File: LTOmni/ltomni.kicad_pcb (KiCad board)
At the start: 2 copper layers, 114.3 x 76.2 mm, 136 parts, among them J1 USB_C_Receptacle, J2 USB_C_Receptacle, J3 TC2030-IDC, J4 D4, J5 D5, J6 A6, J7 A7, J8 B0, K0 K00, K1 K01, K10 K10, K10b1 K10b, K11 K11, K12 K12, K13 K13, K14 K14, K15 K15, K15b1 K15b, K2 K02, K20 K20, K21 K21, K22 K22, K23 K23, K24 K24, K25 K25, K3 K03, K30 K30, K30b1 K30b, K30b2 K30b2, K31 K31, K31b2 K31b, K31c1 K31c, K32 K32, K32b1 K32b1, K32b2 K32b2, K33 K33, K33b1 K33b, K34 K34, K34b1 K34b, K34c1 K34c, K35 K35, K35b1 K35b, K35c2 K35c, K4 K04, K5 K05, SW1 Switch-6P-2S2T, SW2 SW_Push, U1 MCP73831, U2 MCP1700 (3.0V), U3 MCP1700 (3.3V), U4 ATXMEGA-A4U-EPAD, U5 74LVC1G34, U6 nRF24L01_module, U7 FSUSB42, U8 FSUSB42, U9 FSUSB42

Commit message: Before adding rotary encoders
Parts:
- removed C11, C12, C13, C14, C15, C16, C17, C8, C9: 0.1uF, Capacitor_SMD:C_0805_2012Metric
- removed LED1, LED10, LED2, LED3, LED4, LED5, LED6, LED7, LED8, LED9: WS2812B, LED_SMD:LED_WS2812B_PLCC4_5.0x5.0mm_P3.2mm
- removed SW1: Switch-6P-2S2T, Button_Switch_THT:SW_CuK_JS202011CQN_DPDT_Straight
- added PWR1: Switch-6P-2S2T, Button_Switch_THT:SW_CuK_JS202011CQN_DPDT_Straight, F.Cu at (54.9, 55.3)
- added RGB1: Conn_01x03_Male, Connector_PinHeader_1.27mm:PinHeader_1x03_P1.27mm_Vertical, F.Cu at (26.6, 20.3)
- K10b1, K15b1, K35b1: footprint Button_Switch_Keyboard:SW_Cherry_MX1A_2.00u_Vertical_Plate -> Keebio-Parts:MX_PCB_200V
- K30b2, K32b1: footprint Button_Switch_Keyboard:SW_Cherry_MX1A_2.00u_Plate -> Keebio-Parts:MX_PCB_200H
- U4: footprint Package_QFP:TQFP-44-1EP_10x10mm_P0.8mm_EP4.5x4.5mm -> Package_QFP:TQFP-44_10x10mm_P0.8mm
- moved D20 19.8 mm to (91.2, 69.8)
- moved D30 19.5 mm to (91.2, 72.4)
- moved U5 17.5 mm to (30.4, 19.6), turned to 270 degrees
- moved D15 15.9 mm to (18.8, 23.8)
- moved K30b2 12.9 mm to (104.8, 57.1), turned to 90 degrees
- moved K35 11.4 mm to (12.3, 71.8), turned to 0 degrees
- moved D32 9.10 mm to (74.3, 66.3), turned to 270 degrees
- moved K35b1 8.28 mm to (19.1, 66.7), turned to 90 degrees
- moved D24 7.17 mm to (26.1, 53.2)
- moved K10b1 5.68 mm to (104.8, 19.1), turned to 180 degrees
- moved K15b1 5.68 mm to (9.54, 19.1), turned to 0 degrees
- moved K32b1 5.68 mm to (57.2, 66.7), turned to 0 degrees
- moved D_5 3.71 mm to (15.4, 11.6)
- moved D35 3.22 mm to (21.9, 62.2)
- moved D31 2.84 mm to (88.2, 61.2)
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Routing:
- net +5V: track 416.1 -> 98.8 mm, vias 10 -> 4
- net Net-(LED3-Pad2): track 71.1 -> 0.00 mm, vias 4 -> 0
- net Net-(LED2-Pad2): track 59.9 -> 0.00 mm, vias 4 -> 0
- net Net-(LED8-Pad2): track 36.8 -> 0.00 mm, vias 2 -> 0
- net Net-(LED7-Pad2): track 34.7 -> 0.00 mm
- net Net-(LED5-Pad2): track 34.5 -> 0.00 mm
- net Net-(LED10-Pad4): track 31.0 -> 0.00 mm, vias 2 -> 0
- net Net-(LED1-Pad2): track 29.8 -> 0.00 mm, vias 2 -> 0
- net Net-(LED4-Pad2): track 27.6 -> 0.00 mm
- net /COL3: track 103.4 -> 129.2 mm
- net /COL5: track 97.6 -> 122.7 mm, vias 1 -> 0
- net Net-(LED6-Pad2): track 24.7 -> 0.00 mm
- net Net-(D20-Pad2): track 3.18 -> 24.0 mm
- net /UNDER_LED: track 45.9 -> 28.8 mm
- net Net-(D35-Pad2): track 10.9 -> 27.5 mm
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
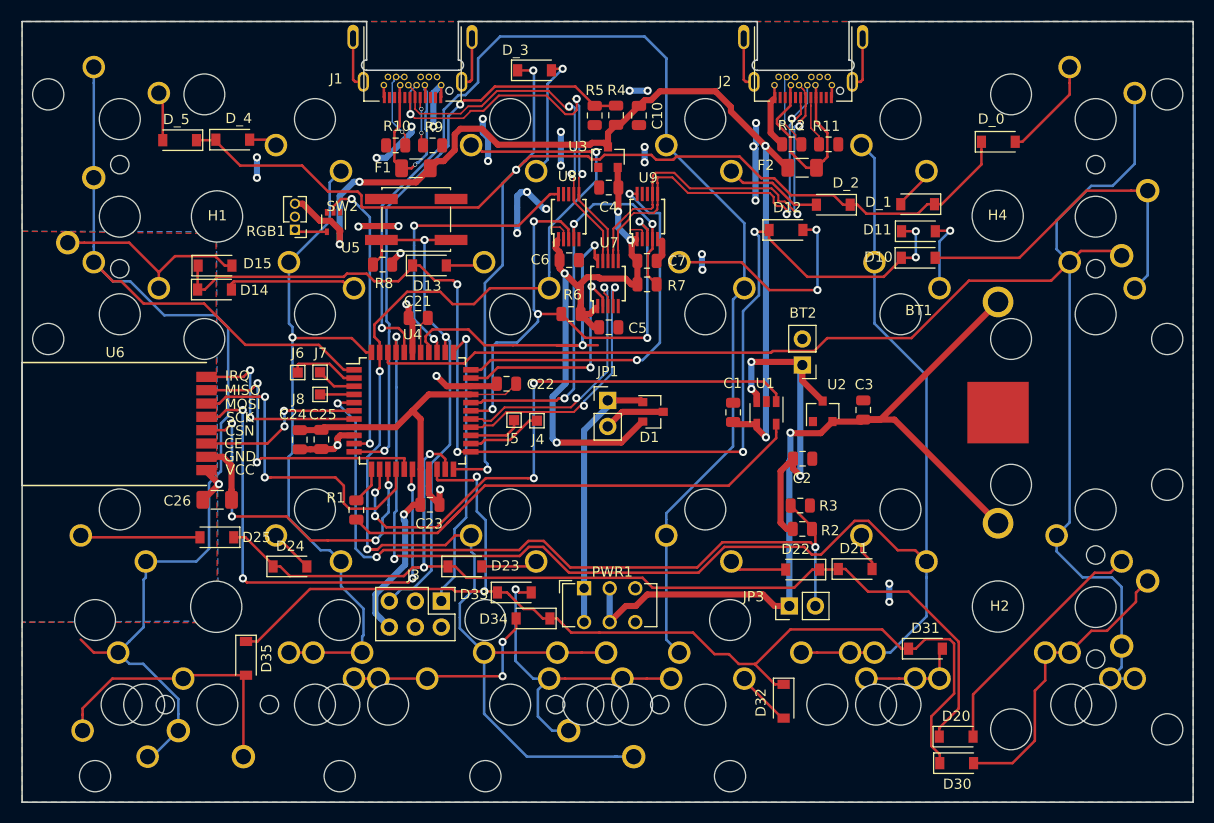
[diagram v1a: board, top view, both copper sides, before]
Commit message: now with rotary encoder
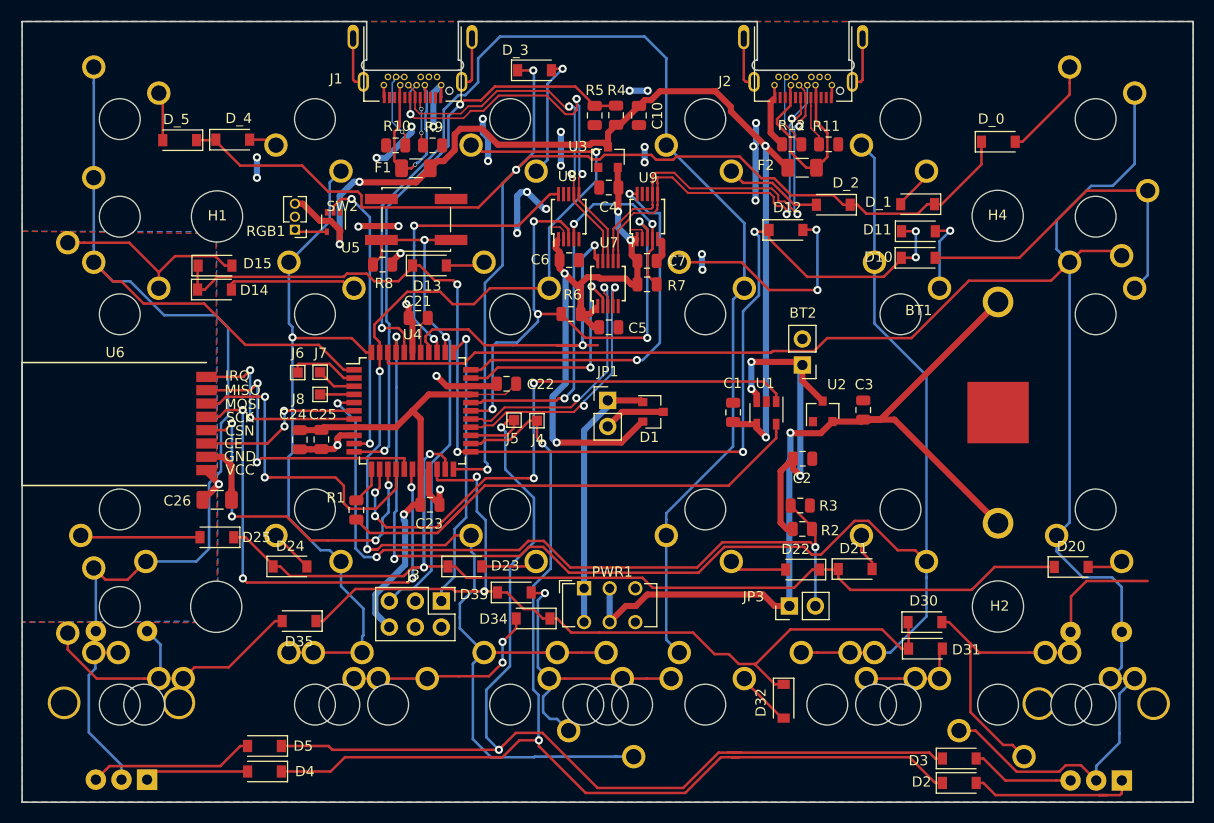
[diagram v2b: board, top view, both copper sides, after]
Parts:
- added D2: D, Diode_SMD:D_SOD-123, F.Cu at (91.5, 74.3)
- added D3: D, Diode_SMD:D_SOD-123, F.Cu at (91.5, 71.9)
- added D4: D, Diode_SMD:D_SOD-123, F.Cu at (23.7, 73.2)
- added D5: D, Diode_SMD:D_SOD-123, F.Cu at (23.7, 70.7)
- added SW1: Rotary_Encoder_Switch, Rotary_Encoder:RotaryEncoder_Alps_EC11E-Switch_Vertical_H20mm_CircularMountingHoles, B.Cu at (107.3, 74.1)
- added SW3: Rotary_Encoder_Switch, Rotary_Encoder:RotaryEncoder_Alps_EC11E-Switch_Vertical_H20mm_CircularMountingHoles, B.Cu at (12.2, 74.0)
- K0, K1, K10, K11, K12, K13, K14, K15, K2, K20, K21, K22, K23, K24, K25, K3, K30, K31, K32, K33, K34, K35, K4, K5: footprint Button_Switch_Keyboard:SW_Cherry_MX1A_1.00u_Plate -> Keebio-Parts:MX_Plate_100H
- K10b1, K15b1, K35b1: footprint Keebio-Parts:MX_PCB_200V -> Keebio-Parts:MX_Plate_200V
- K30b1, K31b2, K31c1, K32b2, K33b1, K34b1, K34c1, K35c2: footprint Button_Switch_Keyboard:SW_Cherry_MX1A_1.25u_Plate -> Keebio-Parts:MX_Plate_125H
- K30b2, K32b1: footprint Keebio-Parts:MX_PCB_200H -> Keebio-Parts:MX_Plate_200H
- moved D20 20.0 mm to (102.4, 53.2)
- moved D30 14.1 mm to (88.1, 58.6)
- moved K35b1 13.5 mm to (9.54, 57.1), turned to 0 degrees
- moved K30b2 13.5 mm to (95.3, 66.7), turned to 0 degrees
- moved D35 6.33 mm to (27.0, 58.5), turned to 180 degrees
- moved K35 5.76 mm to (9.54, 66.7), turned to 180 degrees
- moved K1 5.68 mm to (85.7, 9.53)
- moved K11 5.68 mm to (85.7, 28.6)
- moved K12 5.68 mm to (66.7, 28.6)
- moved K20 5.68 mm to (104.8, 47.6)
- moved K21 5.68 mm to (85.7, 47.6)
- moved K30b1 5.68 mm to (102.4, 66.7)
- moved K31 5.68 mm to (85.7, 66.7)
- moved K31b2 5.68 mm to (83.4, 66.7)
- moved K31c1 5.68 mm to (78.6, 66.7)
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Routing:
- net /D5: track 5.27 -> 112.6 mm, vias 0 -> 2
- net /D4: track 7.38 -> 111.5 mm, vias 0 -> 2
- net /COL0: track 147.1 -> 174.6 mm
- net /ROW3: track 110.3 -> 87.3 mm
- net Net-(D20-Pad2): track 24.0 -> 3.50 mm
- net Net-(D2-Pad2): track 0.00 -> 16.8 mm
- net Net-(D5-Pad2): track 0.00 -> 16.2 mm
- net Net-(D30-Pad2): track 29.3 -> 41.0 mm
- net Net-(D4-Pad2): track 0.00 -> 10.1 mm
- net Net-(D3-Pad2): track 0.00 -> 10.1 mm
- net /COL5: track 122.7 -> 126.9 mm
- net Net-(D35-Pad2): track 27.5 -> 31.2 mm
- net Net-(D33-Pad2): track 32.5 -> 29.1 mm
- net /COL3: track 129.2 -> 132.2 mm
- net GND: track 114.2 -> 112.4 mm, vias 24 -> 22
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
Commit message: maybe a final design?
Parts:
- SW1, SW3: footprint Rotary_Encoder:RotaryEncoder_Alps_EC11E-Switch_Vertical_H20mm_CircularMountingHoles -> Keebio-Parts:RotaryEncoder_Alps_EC11E-Switch_Vertical_H20mm_CircularMountingHoles
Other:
- board text added: "LTOmni Alpha-1"
- board text added: "© 2019-01-20 LovesTha"

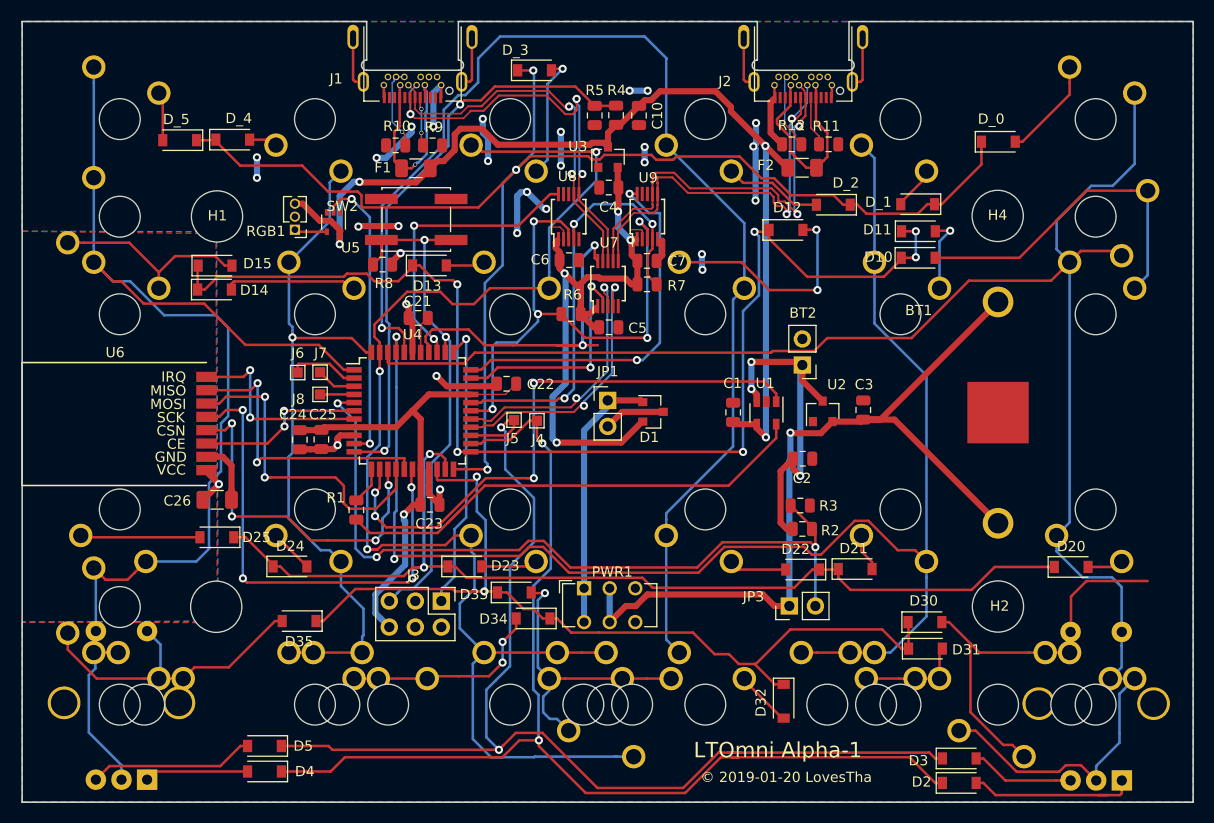
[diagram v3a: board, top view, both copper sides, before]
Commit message: Rotated the diodes to all be the same way around
Also added switch labels on the back, might be too many labels.
Title and copyright moved to top left corner.
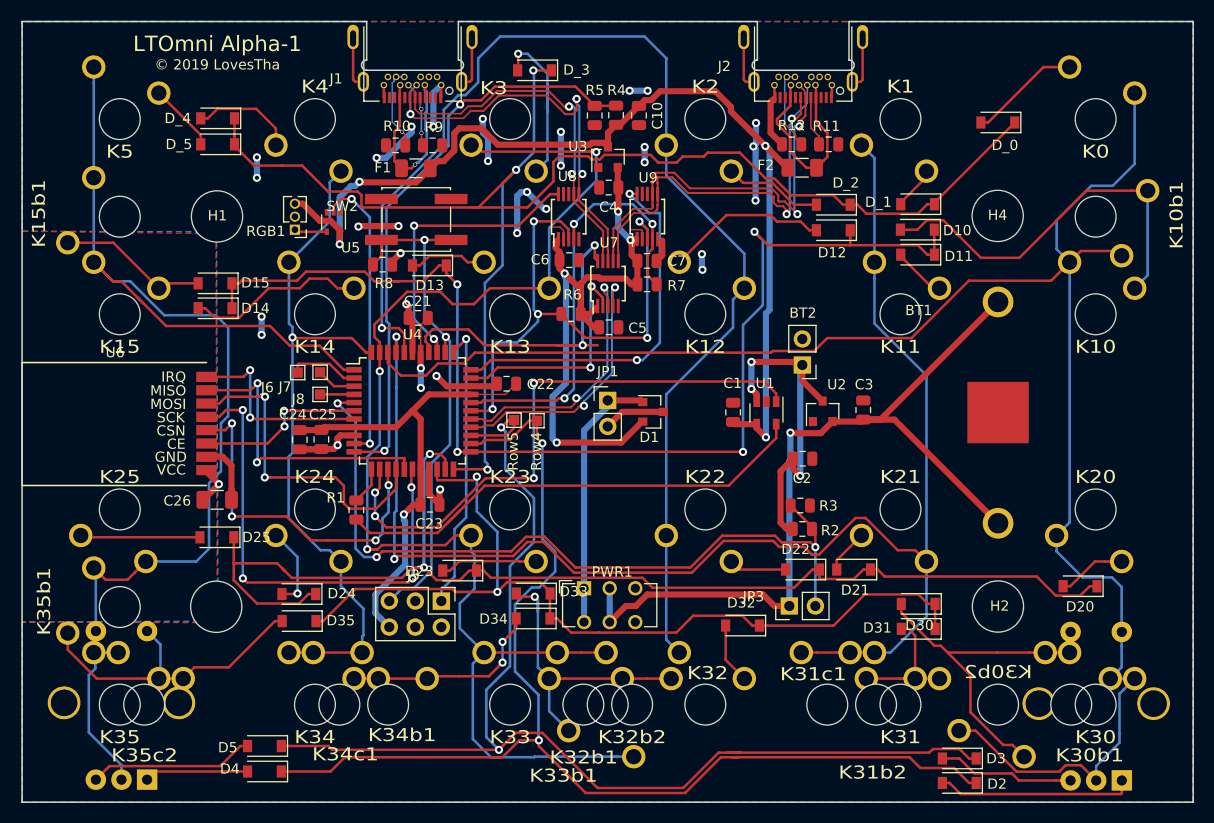
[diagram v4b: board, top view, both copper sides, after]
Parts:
- moved D32 8.40 mm to (70.3, 59.0), turned to 180 degrees
- moved D12 4.62 mm to (79.2, 20.4), turned to 180 degrees
- moved D_5 3.73 mm to (19.1, 12.0)
- moved D24 2.83 mm to (27.0, 55.9), turned to 180 degrees
- moved D10 2.74 mm to (87.4, 20.3), turned to 180 degrees
- moved D_4 2.55 mm to (19.1, 9.45), turned to 180 degrees
- moved D11 2.29 mm to (87.4, 22.8), turned to 180 degrees
- moved D20 2.07 mm to (103.3, 55.1), turned to 180 degrees
- moved D31 2.06 mm to (87.5, 59.3), turned to 180 degrees
- moved D30 1.90 mm to (87.5, 56.8), turned to 180 degrees
- moved D_0 1.88 mm to (95.2, 9.86), turned to 180 degrees
- moved D33 1.85 mm to (49.9, 55.8), turned to 180 degrees
- moved D14 1.83 mm to (18.8, 28.0), turned to 180 degrees
- moved D15 1.73 mm to (18.8, 25.6), turned to 180 degrees
- moved D23 0.65 mm to (42.7, 53.6), turned to 180 degrees
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- renumbered J4 to Row4, J5 to Row5
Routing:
- net /ROW2: track 109.6 -> 127.7 mm
- net /ROW0: track 135.3 -> 144.5 mm
- net Net-(D_4-Pad2): track 2.79 -> 10.1 mm
- net Net-(D30-Pad2): track 41.0 -> 34.6 mm
- net Net-(D12-Pad2): track 21.9 -> 15.9 mm, vias 2 -> 0
- net Net-(D_3-Pad2): track 12.2 -> 18.0 mm
- net /D4: track 111.5 -> 117.0 mm
- net Net-(D10-Pad2): track 33.5 -> 38.8 mm
- net GND: track 112.4 -> 117.7 mm, vias 22 -> 26
- net Net-(D15-Pad2): track 19.8 -> 14.8 mm
- net Net-(D14-Pad2): track 12.9 -> 17.6 mm
- net Net-(D23-Pad2): track 5.51 -> 9.52 mm
- net Net-(D13-Pad2): track 3.82 -> 7.77 mm
- net Net-(D31-Pad2): track 10.2 -> 14.1 mm
- net Net-(D24-Pad2): track 4.27 -> 8.08 mm, vias 0 -> 1
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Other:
- board text added: "© 2019 LovesTha"
- board text removed: "© 2019-01-20 LovesTha"
